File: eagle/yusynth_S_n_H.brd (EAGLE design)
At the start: 100.8 x 81 mm, 43 parts, among them IC1 TL074P, IC2 TL071P, Q1 BF245, T1 2N3904

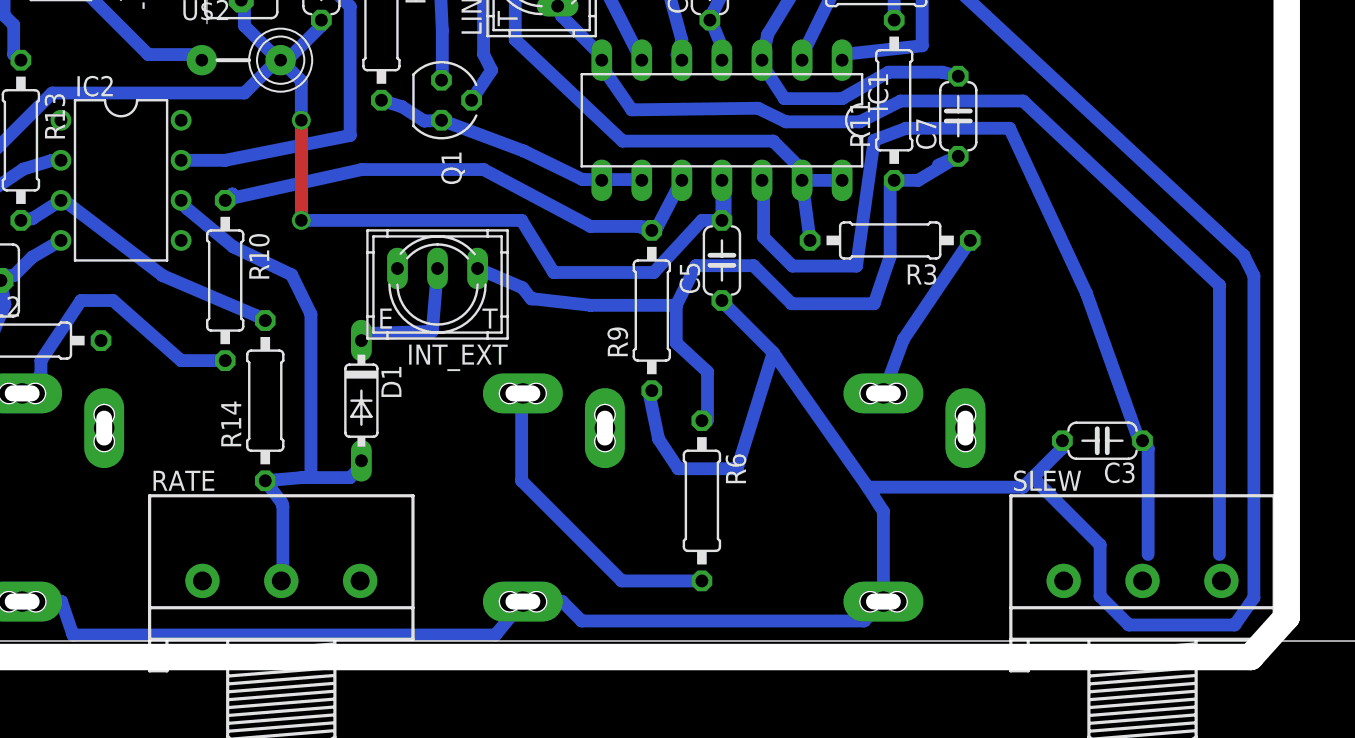
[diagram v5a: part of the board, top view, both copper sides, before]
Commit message: routed to reflect last schemo changes
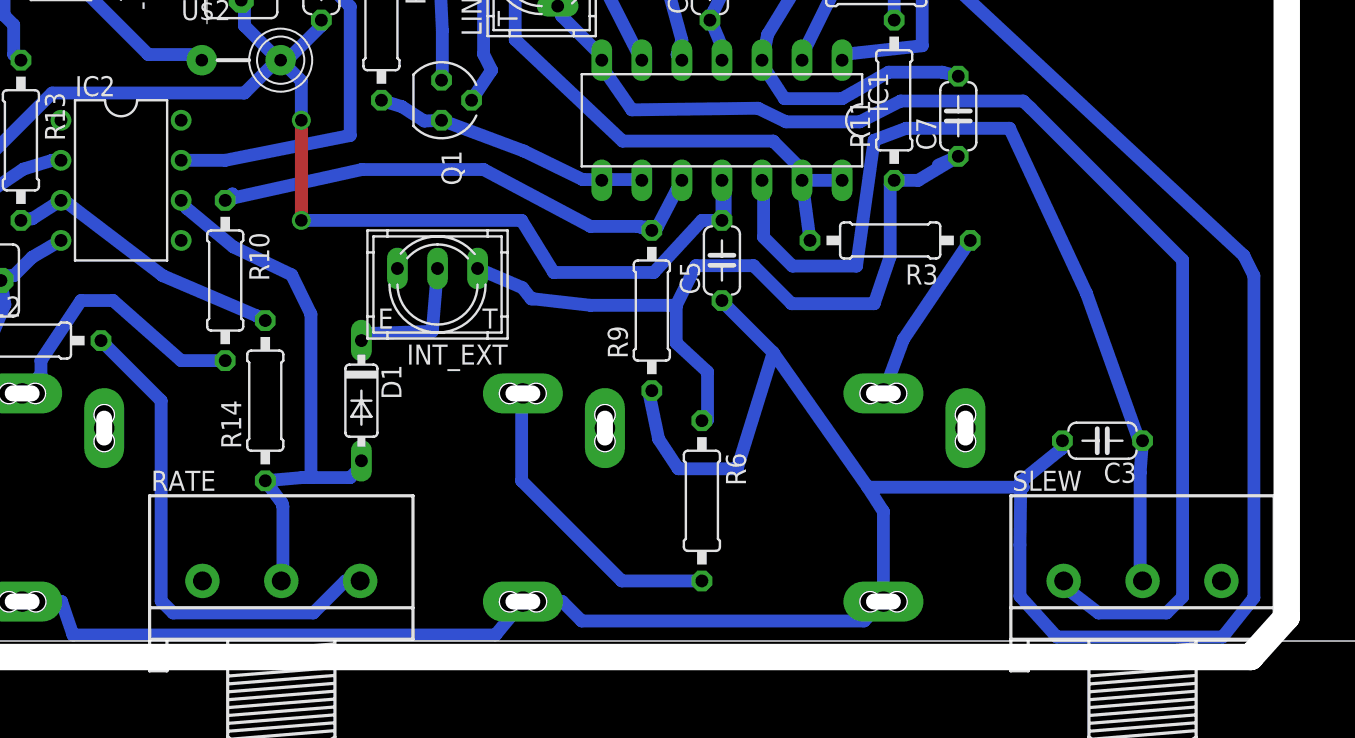
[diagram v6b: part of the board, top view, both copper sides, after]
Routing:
- net N$12: track 0.00 -> 31.9 mm
- net N$19: track 67.8 -> 78.2 mm
- net GND: track 372.6 -> 376.7 mm
- net N$13: track 56.0 -> 57.4 mm
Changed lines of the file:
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@@
 <wire x1="57.3532" y1="18.288" x2="54.3052" y2="21.336" width="0.8128" layer="16"/>
 <wire x1="73.2028" y1="9.7536" x2="63.3476" y2="9.7536" width="0.8128" layer="16"/>
-<wire x1="75.6412" y1="12.192" x2="73.8124" y2="10.3632" width="0.8128" layer="16"/>
-<wire x1="73.8124" y1="10.3632" x2="73.2028" y2="9.7536" width="0.8128" layer="16"/>
+<wire x1="75.6412" y1="12.192" x2="73.0504" y2="10.1092" width="0.8128" layer="16"/>
+<wire x1="73.0504" y1="10.1092" x2="73.2028" y2="9.7536" width="0.8128" layer="16"/>
 <wire x1="54.3052" y1="21.336" x2="54.102" y2="21.59" width="0.8128" layer="16"/>
 <wire x1="75.6412" y1="12.192" x2="75.692" y2="12.7" width="0.8128" layer="16"/>
@@
 <wire x1="57.3532" y1="18.288" x2="55.0672" y2="10.922" width="0.8128" layer="16"/>
 <wire x1="87.8332" y1="2.7432" x2="87.8332" y2="23.1648" width="0.8128" layer="16"/>
-<wire x1="86.614" y1="1.016" x2="87.8332" y2="2.7432" width="0.8128" layer="16"/>
-<wire x1="79.9084" y1="1.016" x2="86.614" y2="1.016" width="0.8128" layer="16"/>
-<wire x1="78.0796" y1="2.8448" x2="79.9084" y2="1.016" width="0.8128" layer="16"/>
-<wire x1="78.0796" y1="6.096" x2="78.0796" y2="2.8448" width="0.8128" layer="16"/>
-<wire x1="73.8124" y1="10.3632" x2="78.0796" y2="6.096" width="0.8128" layer="16"/>
+<wire x1="85.852" y1="0.254" x2="87.8332" y2="2.7432" width="0.8128" layer="16"/>
+<wire x1="75.3364" y1="0.254" x2="85.852" y2="0.254" width="0.8128" layer="16"/>
+<wire x1="72.9996" y1="2.8448" x2="75.3364" y2="0.254" width="0.8128" layer="16"/>
+<wire x1="72.9996" y1="6.096" x2="72.9996" y2="2.8448" width="0.8128" layer="16"/>
+<wire x1="73.0504" y1="10.1092" x2="72.9996" y2="6.096" width="0.8128" layer="16"/>
 <wire x1="40.8432" y1="53.086" x2="40.8432" y2="53.594" width="0.8128" layer="16"/>
 <wire x1="40.8432" y1="53.594" x2="40.894" y2="53.6448" width="0.8128" layer="16"/>
@@
 <wire x1="87.8332" y1="23.1648" x2="87.1982" y2="24.4348" width="0.8128" layer="16"/>
 <wire x1="87.1982" y1="24.4348" x2="68.961" y2="41.402" width="0.8128" layer="16"/>
-<wire x1="49.4538" y1="15.8496" x2="49.657" y2="15.875" width="0" layer="19" extent="16-16"/>
 <wire x1="68.961" y1="41.402" x2="70.358" y2="41.402" width="0.8128" layer="16"/>
 <wire x1="70.358" y1="41.402" x2="72.898" y2="43.942" width="0.8128" layer="16"/>
+<wire x1="49.4538" y1="15.8496" x2="49.657" y2="15.875" width="0" layer="19" extent="16-16"/>
 </signal>
 <signal name="N$14">
@@
 <contactref element="IC1" pad="12"/>
 <contactref element="C3" pad="1"/>
-<wire x1="81.1276" y1="5.4864" x2="81.1276" y2="12.192" width="0.8128" layer="16"/>
-<wire x1="81.1276" y1="12.192" x2="80.772" y2="12.7" width="0.8128" layer="16"/>
+<wire x1="80.6196" y1="3.9624" x2="80.6196" y2="10.668" width="0.8128" layer="16"/>
+<wire x1="80.6196" y1="10.668" x2="80.772" y2="12.7" width="0.8128" layer="16"/>
 <wire x1="56.7436" y1="25.6032" x2="56.7436" y2="28.6512" width="0.8128" layer="16"/>
 <wire x1="58.5724" y1="23.7744" x2="56.7436" y2="25.6032" width="0.8128" layer="16"/>
@@
 <wire x1="80.518" y1="12.8016" x2="80.772" y2="12.7" width="0.8128" layer="16"/>
 <contactref element="SLEW" pad="2"/>
-<wire x1="80.772" y1="3.81" x2="81.1276" y2="5.4864" width="0" layer="19" extent="16-16"/>
+<wire x1="80.772" y1="3.81" x2="80.6196" y2="3.9624" width="0" layer="19" extent="16-16"/>
 </signal>
 <signal name="N$19">
@@
 <wire x1="43.688" y1="40.1828" x2="43.688" y2="40.259" width="0.8128" layer="16"/>
 <wire x1="46.3804" y1="37.1856" x2="46.482" y2="36.83" width="0.8128" layer="16"/>
-<wire x1="85.6488" y1="22.5552" x2="85.6488" y2="5.4864" width="0.8128" layer="16"/>
-<wire x1="73.2028" y1="34.2392" x2="85.6488" y2="22.5552" width="0.8128" layer="16"/>
+<wire x1="73.2028" y1="34.2392" x2="73.67396875" y2="33.796878125" width="0.8128" layer="16"/>
 <wire x1="65.4304" y1="34.2392" x2="73.2028" y2="34.2392" width="0.8128" layer="16"/>
 <wire x1="62.8396" y1="32.9184" x2="65.4304" y2="34.2392" width="0.8128" layer="16"/>
@@
 <wire x1="46.3804" y1="36.576" x2="46.482" y2="36.83" width="0.8128" layer="16"/>
 <contactref element="SLEW" pad="1"/>
-<wire x1="75.772" y1="3.81" x2="85.6488" y2="5.4864" width="0" layer="19" extent="16-16"/>
+<wire x1="75.772" y1="3.81" x2="75.772" y2="3.476" width="0.8128" layer="16"/>
+<wire x1="75.772" y1="3.476" x2="77.978" y2="1.778" width="0.8128" layer="16"/>
+<wire x1="77.978" y1="1.778" x2="82.296" y2="1.778" width="0.8128" layer="16"/>
+<wire x1="82.296" y1="1.778" x2="83.312" y2="2.794" width="0.8128" layer="16"/>
+<wire x1="83.312" y1="2.794" x2="83.312" y2="24.158846875" width="0.8128" layer="16"/>
+<wire x1="83.312" y1="24.158846875" x2="73.67396875" y2="33.796878125" width="0.8128" layer="16"/>
 </signal>
 <signal name="N$20">
@@
 <contactref element="RATE" pad="3"/>
 <contactref element="R12" pad="2"/>
-<wire x1="14.732" y1="19.05" x2="31.162" y2="3.81" width="0" layer="19" extent="1-1"/>
+<wire x1="31.162" y1="3.81" x2="30.226" y2="3.81" width="0.8128" layer="16"/>
+<wire x1="30.226" y1="3.81" x2="28.194" y2="1.778" width="0.8128" layer="16"/>
+<wire x1="28.194" y1="1.778" x2="19.304" y2="1.778" width="0.8128" layer="16"/>
+<wire x1="19.304" y1="1.778" x2="18.542" y2="2.54" width="0.8128" layer="16"/>
+<wire x1="18.542" y1="2.54" x2="18.542" y2="15.24" width="0.8128" layer="16"/>
+<wire x1="18.542" y1="15.24" x2="14.732" y2="19.05" width="0.8128" layer="16"/>
 </signal>
 </signals>
